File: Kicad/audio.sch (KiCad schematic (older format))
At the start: 71 parts, among them J601 CD Audio In, J602 AC'97 Audio Header, J603 Line Out, U601 TLV320AIC23BPW, U602 STX-4335-5BGP-S1, Y601 12M

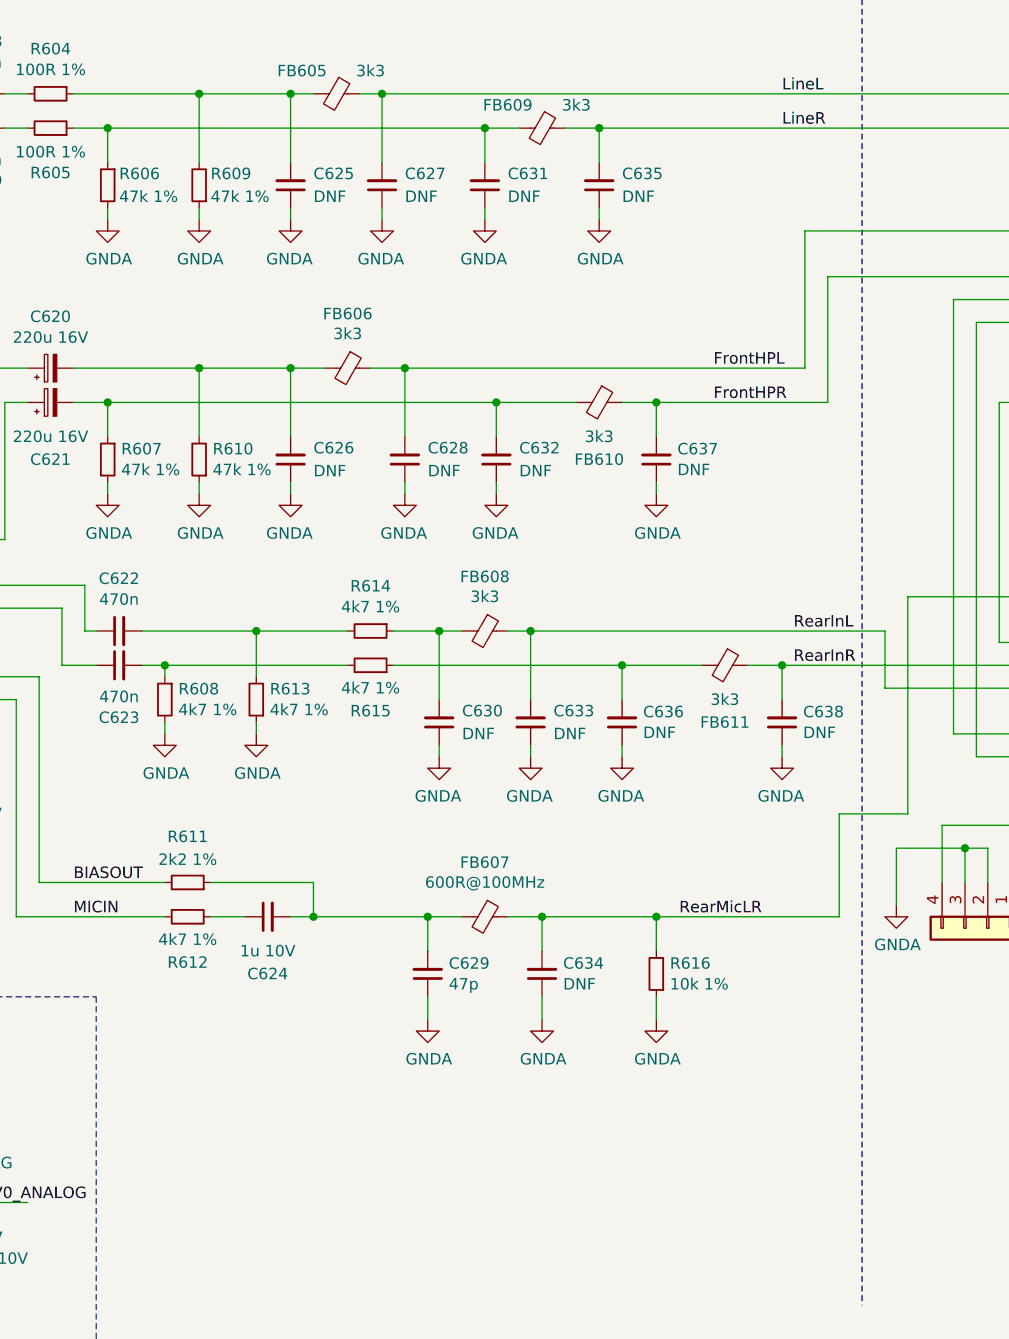
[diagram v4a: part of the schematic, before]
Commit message: Changes to BMC
* Swapped BUTTON_PWR and SYS_RESET to avoid DRC issue
* Split PSU and BMC into two separate sheets
* Swapped some pins on the STM32 to make it compatible with more
alternatives
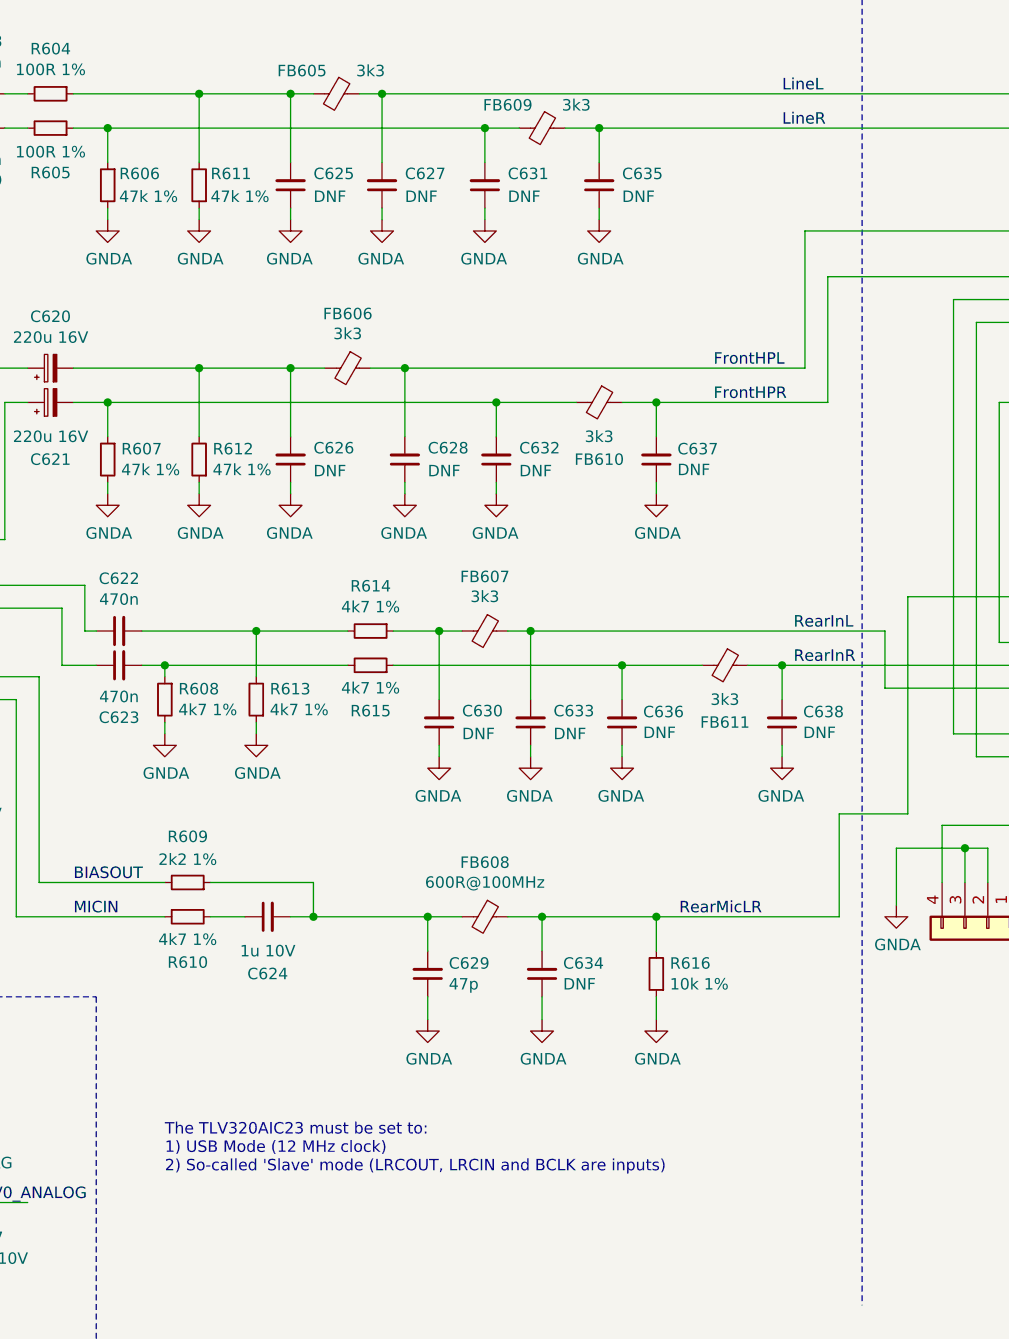
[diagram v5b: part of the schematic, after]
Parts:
- renumbered FB608 to FB607, FB607 to FB608, R611 to R609, R612 to R610, R609 to R611, R610 to R612
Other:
- note added: "The TLV320AIC23 must be set to:\n1) USB Mode (12 MHz clock)\n2) So-called 'Slave' mode (LRCOUT, LRCIN and BCLK are inputs)"
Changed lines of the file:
@@
 $Descr A4 11693 8268
 encoding utf-8
-Sheet 6 16
+Sheet 6 17
 Title "Neotron Common Hardware - Audio CODEC"
 Date "2021-04-02"
@@
 $EndComp
 $Comp
-L Device:R_Small R609
+L Device:R_Small R611
 U 1 1 5FEF713B
 P 5250 1650
-F 0 "R609" H 5200 1600 50  0000 R CNN
+F 0 "R611" H 5200 1600 50  0000 R CNN
 F 1 "47k 1%" H 5200 1700 50  0000 R CNN
 F 2 "Resistor_SMD:R_0805_2012Metric_Pad1.20x1.40mm_HandSolder" H 5250 1650 50  0001 C CNN
@@
 $EndComp
 $Comp
-L Device:R_Small R610
+L Device:R_Small R612
 U 1 1 6000BE6E
 P 5250 2850
-F 0 "R610" H 5191 2804 50  0000 R CNN
+F 0 "R612" H 5191 2804 50  0000 R CNN
 F 1 "47k 1%" H 5191 2895 50  0000 R CNN
 F 2 "Resistor_SMD:R_0805_2012Metric_Pad1.20x1.40mm_HandSolder" H 5250 2850 50  0001 C CNN
@@
 $EndComp
 $Comp
-L Device:R_Small R612
+L Device:R_Small R610
 U 1 1 605E8027
 P 5200 4850
-F 0 "R612" V 5400 4850 50  0000 C CNN
+F 0 "R610" V 5400 4850 50  0000 C CNN
 F 1 "4k7 1%" V 5300 4850 50  0000 C CNN
 F 2 "Resistor_SMD:R_0805_2012Metric_Pad1.20x1.40mm_HandSolder" H 5200 4850 50  0001 C CNN
@@
 $EndComp
 $Comp
-L Device:R_Small R611
+L Device:R_Small R609
 U 1 1 60601172
 P 5200 4700
-F 0 "R611" V 5400 4700 50  0000 C CNN
+F 0 "R609" V 5400 4700 50  0000 C CNN
 F 1 "2k2 1%" V 5300 4700 50  0000 C CNN
 F 2 "Resistor_SMD:R_0805_2012Metric_Pad1.20x1.40mm_HandSolder" H 5200 4700 50  0001 C CNN
@@
 	5750 4700 5750 4850
 $Comp
-L Device:Ferrite_Bead_Small FB607
+L Device:Ferrite_Bead_Small FB608
 U 1 1 606D01FF
 P 6500 4850
-F 0 "FB607" V 6263 4850 50  0000 C CNN
+F 0 "FB608" V 6263 4850 50  0000 C CNN
 F 1 "600R@100MHz" V 6350 4850 50  0000 C CNN
 F 2 "Inductor_SMD:L_0805_2012Metric_Pad1.15x1.40mm_HandSolder" V 6430 4850 50  0001 C CNN
@@
 	6100 3750 7100 3750
 $Comp
-L Device:Ferrite_Bead_Small FB608
+L Device:Ferrite_Bead_Small FB607
 U 1 1 605225C2
 P 6500 3600
-F 0 "FB608" V 6263 3600 50  0000 C CNN
+F 0 "FB607" V 6263 3600 50  0000 C CNN
 F 1 "3k3" V 6350 3600 50  0000 C CNN
 F 2 "Inductor_SMD:L_0805_2012Metric_Pad1.15x1.40mm_HandSolder" V 6430 3600 50  0001 C CNN
@@
 Wire Wire Line
 	7100 3750 7450 3750
+Text Notes 5100 5975 0    50   ~ 0
+The TLV320AIC23 must be set to:\n1) USB Mode (12 MHz clock)\n2) So-called 'Slave' mode (LRCOUT, LRCIN and BCLK are inputs)
 $EndSCHEMATC

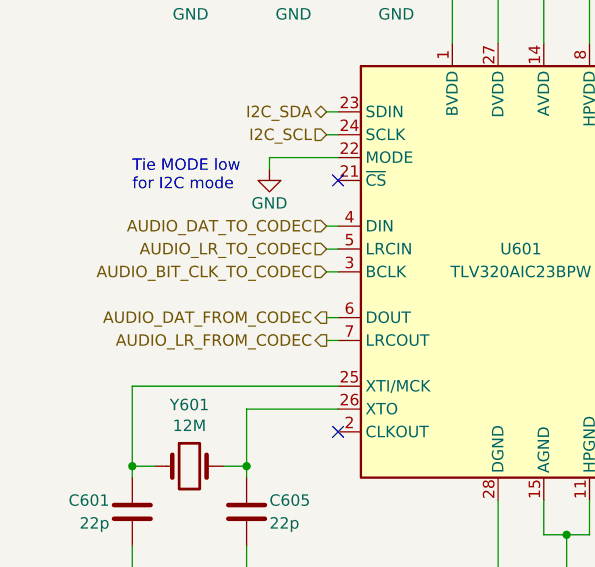
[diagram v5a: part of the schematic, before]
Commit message: Set LR and BCLK on Audio.sch to be bi-directional
In Controller mode these pins are outputs. In peripheral
mode these pins are inputs.
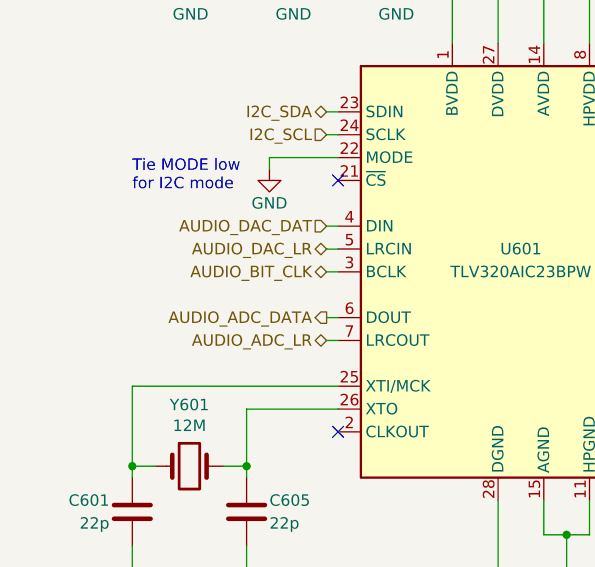
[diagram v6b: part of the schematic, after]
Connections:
- net AUDIO_BIT_CLK_TO_CODEC renamed AUDIO_BIT_CLK
- net AUDIO_DAT_FROM_CODEC renamed AUDIO_ADC_DATA
- net AUDIO_DAT_TO_CODEC renamed AUDIO_DAC_DAT
- net AUDIO_LR_FROM_CODEC renamed AUDIO_ADC_LR
- net AUDIO_LR_TO_CODEC renamed AUDIO_DAC_LR
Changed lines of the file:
@@
 NoConn ~ 9500 4350
 Text HLabel 1850 3300 0    50   Input ~ 0
-AUDIO_DAT_TO_CODEC
-Text HLabel 1850 3400 0    50   Input ~ 0
-AUDIO_LR_TO_CODEC
-Text HLabel 1850 3500 0    50   Input ~ 0
-AUDIO_BIT_CLK_TO_CODEC
+AUDIO_DAC_DAT
+Text HLabel 1850 3400 0    50   BiDi ~ 0
+AUDIO_DAC_LR
+Text HLabel 1850 3500 0    50   BiDi ~ 0
+AUDIO_BIT_CLK
 Text HLabel 1850 3700 0    50   Output ~ 0
-AUDIO_DAT_FROM_CODEC
-Text HLabel 1850 3800 0    50   Output ~ 0
-AUDIO_LR_FROM_CODEC
+AUDIO_ADC_DATA
+Text HLabel 1850 3800 0    50   BiDi ~ 0
+AUDIO_ADC_LR
 $Comp
 L power:GND #PWR0608

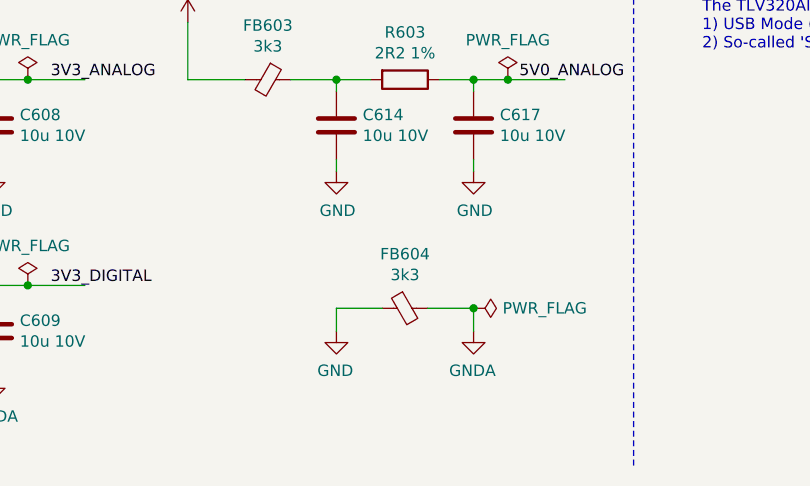
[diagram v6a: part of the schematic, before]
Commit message: Join GNDA and GND on audio sheet.
Most guides recommend against having a split ground, and it certainly
makes layout harder.
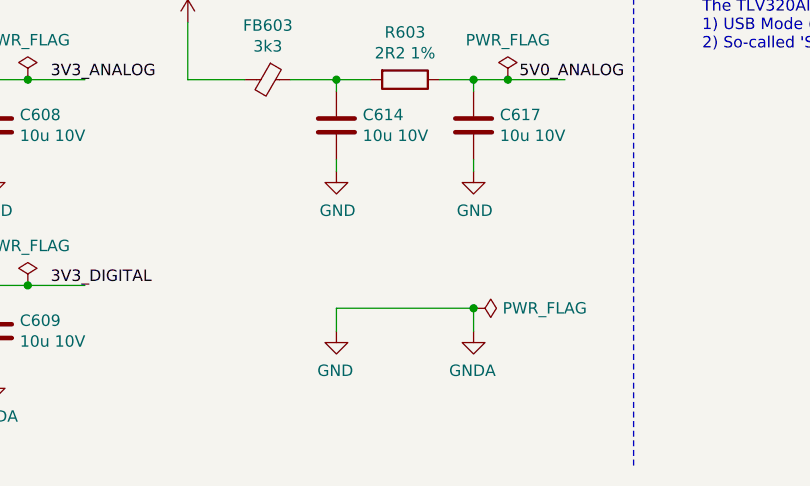
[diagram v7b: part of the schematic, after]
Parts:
- removed FB604: 3k3, Inductor_SMD:L_0805_2012Metric_Pad1.15x1.40mm_HandSolder, symbol Device:Ferrite_Bead_Small
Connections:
- net GNDA is gone; now on net GND: C604.2, C606.2, C609.2, C610.2, C612.2, C613.2, C615.2, C616.2, C625.1, C626.1, C627.1, C628.1, C629.1, C630.1, C631.1, C632.1, C633.1, C634.1, C635.1, C636.1, C637.1, C638.1, J601.2 (Pin_2), J601.3 (Pin_3), J602.2 (Pin_2), J602.4 (Pin_4), J603.2 (Pin_2), J603.3 (Pin_3), R606.2, R607.2, R608.2, R611.1, R612.1, R613.1, R616.1, U601.11 (HPGND), U601.15 (AGND), U602.1 (Sleeve)
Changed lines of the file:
@@
 	-1   0    0    -1
 $EndComp
-$Comp
-L Device:Ferrite_Bead_Small FB604
-U 1 1 601EBC02
-P 3800 7100
-F 0 "FB604" V 3563 7100 50  0000 C CNN
-F 1 "3k3" V 3654 7100 50  0000 C CNN
-F 2 "Inductor_SMD:L_0805_2012Metric_Pad1.15x1.40mm_HandSolder" V 3730 7100 50  0001 C CNN
-F 3 "https://www.murata.com/en-us/products/en-us/products/productdata/8796738977822/ENFA0005.pdf" H 3800 7100 50  0001 C CNN
-F 4 "BLM21PG221SN1D " H 3800 7100 50  0001 C CNN "MPN"
-F 5 "0" H 3800 7100 50  0001 C CNN "DNP"
-F 6 "490-1054-1-ND" H 3800 7100 50  0001 C CNN "Digikey"
-F 7 "Murata" H 3800 7100 50  0001 C CNN "Manufacturer"
-F 8 "81-BLM21P221SG" H 3800 7100 50  0001 C CNN "Mouser"
-	1    3800 7100
-	0    -1   1    0
-$EndComp
 Wire Wire Line
 	4100 7200 4100 7100
 Wire Wire Line
-	4100 7100 3900 7100
-Wire Wire Line
 	3500 7100 3500 7200
-Wire Wire Line
-	3700 7100 3500 7100
 $Comp
 L power:+3V3 #PWR0601
@@
 Text Notes 5100 5975 0    50   ~ 0
 The TLV320AIC23 must be set to:\n1) USB Mode (12 MHz clock)\n2) So-called 'Slave' mode (LRCOUT, LRCIN and BCLK are inputs)
+Wire Wire Line
+	3500 7100 4100 7100
 $EndSCHEMATC

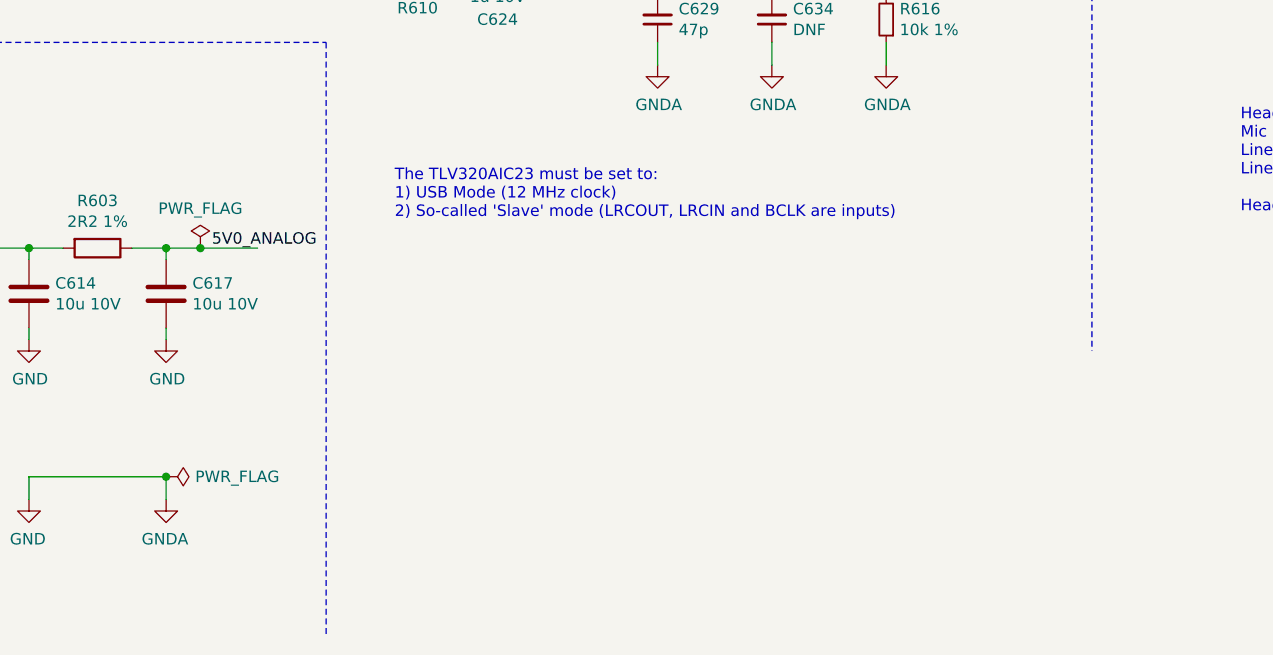
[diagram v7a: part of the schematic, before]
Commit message: Revised PSU switch-on circuit.
Updated notes on BMC and Audio sheet.
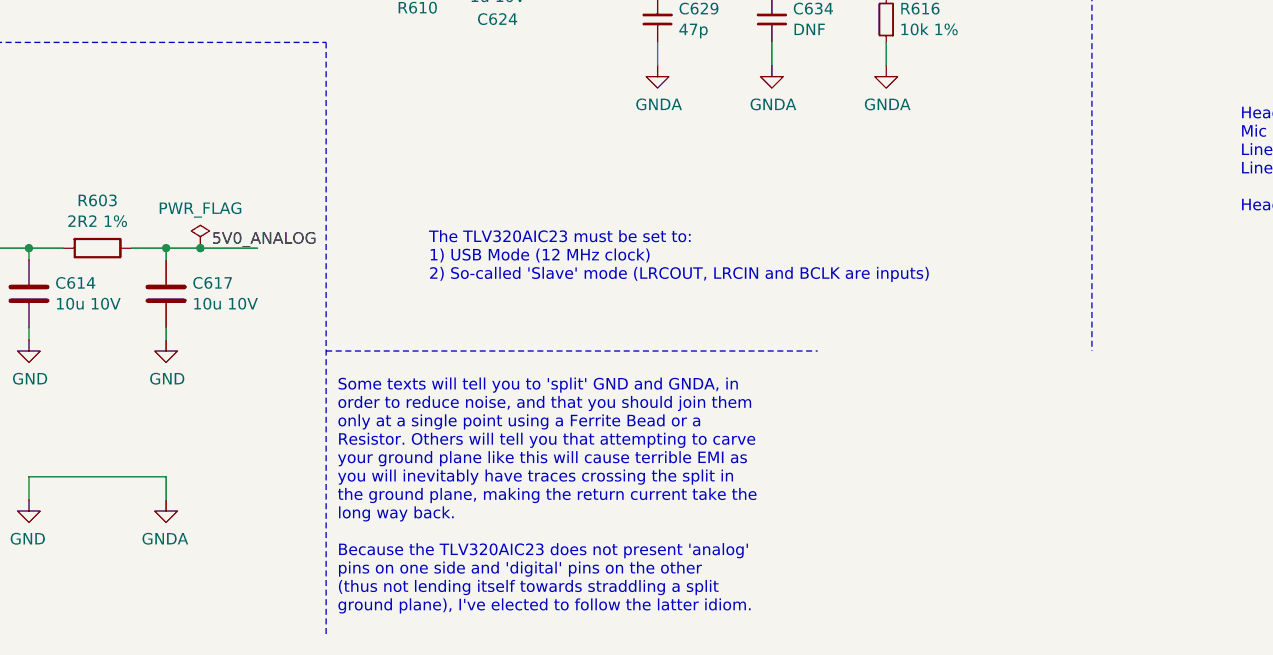
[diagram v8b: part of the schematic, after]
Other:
- note added: "Some texts will tell you to 'split' GND and GNDA, in\norder to reduce noise, and that you should join them\nonly at a single point using a Ferrite Bead or a\nResistor. Others will tell you that attempting to carve\nyour ground plane like this will cause terrible EMI as\nyou will inevitably have traces crossing the split in\nthe ground plane, making the return current take the\nlong way back.\n\nB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"
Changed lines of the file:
@@
 5V0_ANALOG
-$Comp
-L power:PWR_FLAG #FLG0603
-U 1 1 60A6FC05
-P 4100 7100
-F 0 "#FLG0603" H 4100 7175 50  0001 C CNN
-F 1 "PWR_FLAG" V 4100 7227 50  0000 L CNN
-F 2 "" H 4100 7100 50  0001 C CNN
-F 3 "~" H 4100 7100 50  0001 C CNN
-	1    4100 7100
-	0    1    -1   0
-$EndComp
-Connection ~ 4100 7100
 $Comp
 L power:GNDA #PWR0621
@@
 Wire Wire Line
 	7100 3750 7450 3750
-Text Notes 5100 5975 0    50   ~ 0
+Text Notes 5250 6250 0    50   ~ 0
 The TLV320AIC23 must be set to:\n1) USB Mode (12 MHz clock)\n2) So-called 'Slave' mode (LRCOUT, LRCIN and BCLK are inputs)
 Wire Wire Line
 	3500 7100 4100 7100
+Text Notes 4850 7700 0    50   ~ 0
+Some texts will tell you to 'split' GND and GNDA, in\norder to reduce noise, and that you should join them\nonly at a single point using a Ferrite Bead or a\nResistor. Others will tell you that attempting to carve\nyour ground plane like this will cause terrible EMI as\nyou will inevitably have traces crossing the split in\nthe ground plane, making the return current take the\nlong way back.\n\nBecause the TLV320AIC23 does not present 'analog'\npins on one side and 'digital' pins on the other\n(thus not lending itself towards straddling a split\nground plane), I've elected to follow the latter idiom.
+Wire Notes Line
+	4800 6550 6950 6550
 $EndSCHEMATC
